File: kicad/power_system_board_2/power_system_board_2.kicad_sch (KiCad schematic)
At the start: 21 parts, among them J1 USB_C_Receptacle_USB2.0_16P, J2 Conn_01x04_Pin, Q1 NMOS - VN0109N3, Q3 PMOS - VP0106N3, U1 LM358

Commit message: Value updates
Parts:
- R3: value R -> 100K
- R4: value R -> 1.2M // 1.5M
- R5: value R -> 120
- R6: value R -> 90
- R7: value R -> 1M
- R8: value R -> 5M
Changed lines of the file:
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@@
 		(on_board yes)
 		(dnp no)
-		(fields_autoplaced yes)
 		(property "Reference" "R4"
-			(at 91.44 52.0699 0)
+			(at 78.994 51.308 0)
 			(effects
 				(font
@@
 			)
 		)
-		(property "Value" "R"
-			(at 91.44 54.6099 0)
+		(property "Value" "1.2M // 1.5M"
+			(at 73.152 53.34 0)
 			(effects
 				(font
@@
 			)
 		)
-		(property "Value" "R"
+		(property "Value" "120"
 			(at 102.87 68.5799 0)
 			(effects
@@
 		(on_board yes)
 		(dnp no)
-		(fields_autoplaced yes)
 		(property "Reference" "R3"
-			(at 91.44 35.5599 0)
+			(at 83.312 35.052 0)
 			(effects
 				(font
@@
 			)
 		)
-		(property "Value" "R"
-			(at 91.44 38.0999 0)
+		(property "Value" "100K"
+			(at 82.042 36.83 0)
 			(effects
 				(font
@@
 			)
 		)
-		(property "Value" "R"
+		(property "Value" "5M"
 			(at 132.08 54.6099 0)
 			(effects
@@
 			)
 		)
-		(property "Value" "R"
+		(property "Value" "1M"
 			(at 132.08 40.6399 0)
 			(effects
@@
 			)
 		)
-		(property "Value" "R"
+		(property "Value" "90"
 			(at 102.87 34.2899 0)
 			(effects

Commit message: schematic changes
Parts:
- removed R5: 120, symbol Device:R
- removed R7: 1M, symbol Device:R
- removed R8: 5M, symbol Device:R
- R3: value 100K -> 1M + 330k
- R4: value 1.2M // 1.5M -> 2M7 + 220k
- R6: value 90 -> 330
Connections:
- net GND: now also D1.2 (A)
- net at U1.5: now also Q3.2 (G)

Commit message: small changes
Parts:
- added Q2: PMOS - VP0106N3, symbol Simulation_SPICE:PMOS
- added R5: 330, symbol Device:R
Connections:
- net +BATT_UVLO: now also Q2.3 (S); no longer C1.1, C2.1, U3. (OUT)
- net VBUS: now also C1.1, C2.1, U3. (OUT), Q2.1 (D), R5.1
- new net: Q2.2 (G), R5.2
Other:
- note added: "Gate > Source, mosfet is open"

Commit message: Mouse
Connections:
- net -BATT: now also Q1.1 (D); no longer Q1.3 (S)
- net GND: now also Q1.3 (S); no longer Q1.1 (D)
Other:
- moved on the sheet: Q1
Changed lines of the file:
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@@
 	(symbol
 		(lib_id "Simulation_SPICE:NMOS")
-		(at 45.72 36.83 270)
+		(at 45.72 36.83 90)
+		(mirror x)
 		(unit 1)
 		(exclude_from_sim no)
@@
 		)
 		(property "Footprint" ""
-			(at 48.26 41.91 0)
+			(at 43.18 41.91 0)
 			(effects
 				(font
@@
 		)
 		(property "Datasheet" "https://ngspice.sourceforge.io/docs/ngspice-html-manual/manual.xhtml#cha_MOSFETs"
-			(at 33.02 36.83 0)
+			(at 58.42 36.83 0)
 			(effects
 				(font
@@
 		)
 		(property "Sim.Device" "NMOS"
-			(at 28.575 36.83 0)
+			(at 62.865 36.83 0)
 			(effects
 				(font
@@
 		)
 		(property "Sim.Type" "VDMOS"
-			(at 26.67 36.83 0)
+			(at 64.77 36.83 0)
 			(effects
 				(font
@@
 		)
 		(property "Sim.Pins" "1=D 2=G 3=S"
-			(at 30.48 36.83 0)
+			(at 60.96 36.83 0)
 			(effects
 				(font

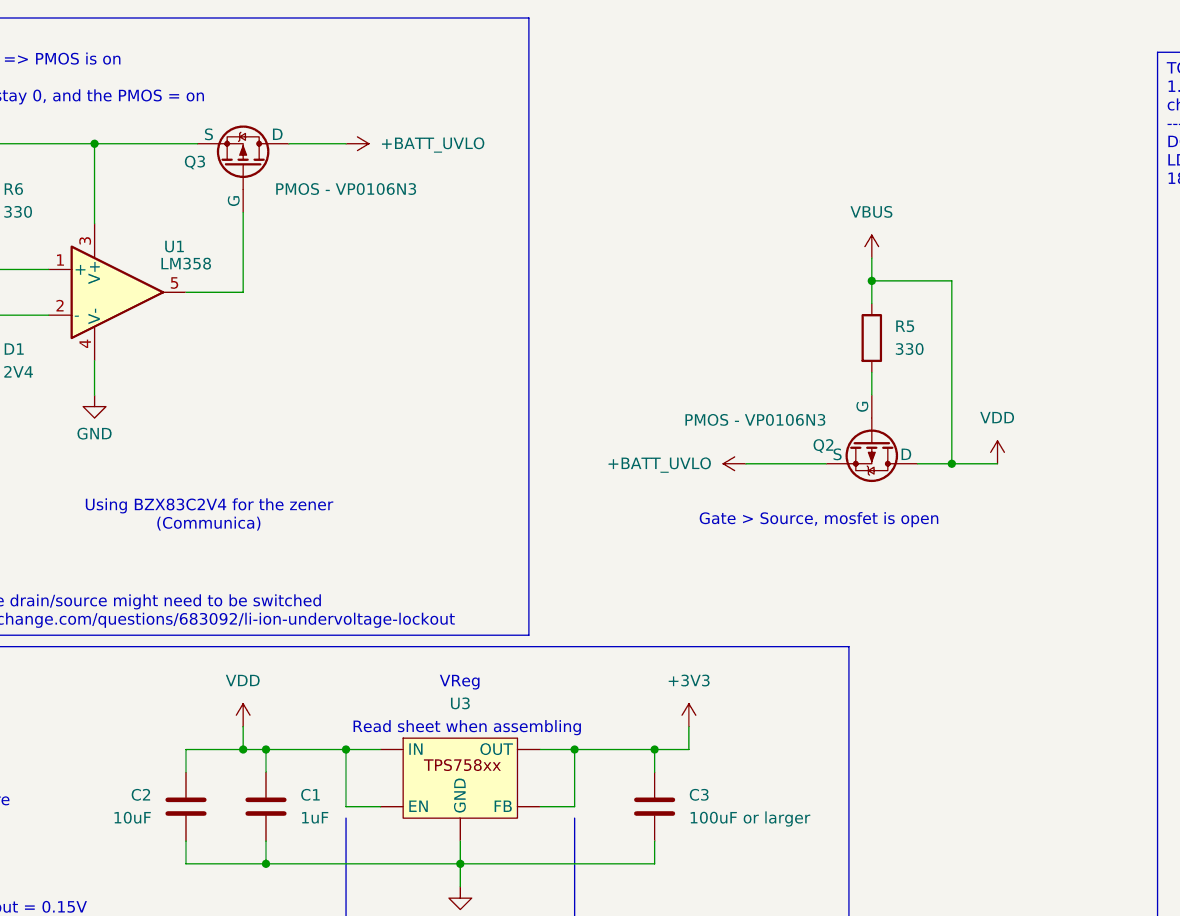
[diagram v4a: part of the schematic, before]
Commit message: Changes to circuit layout
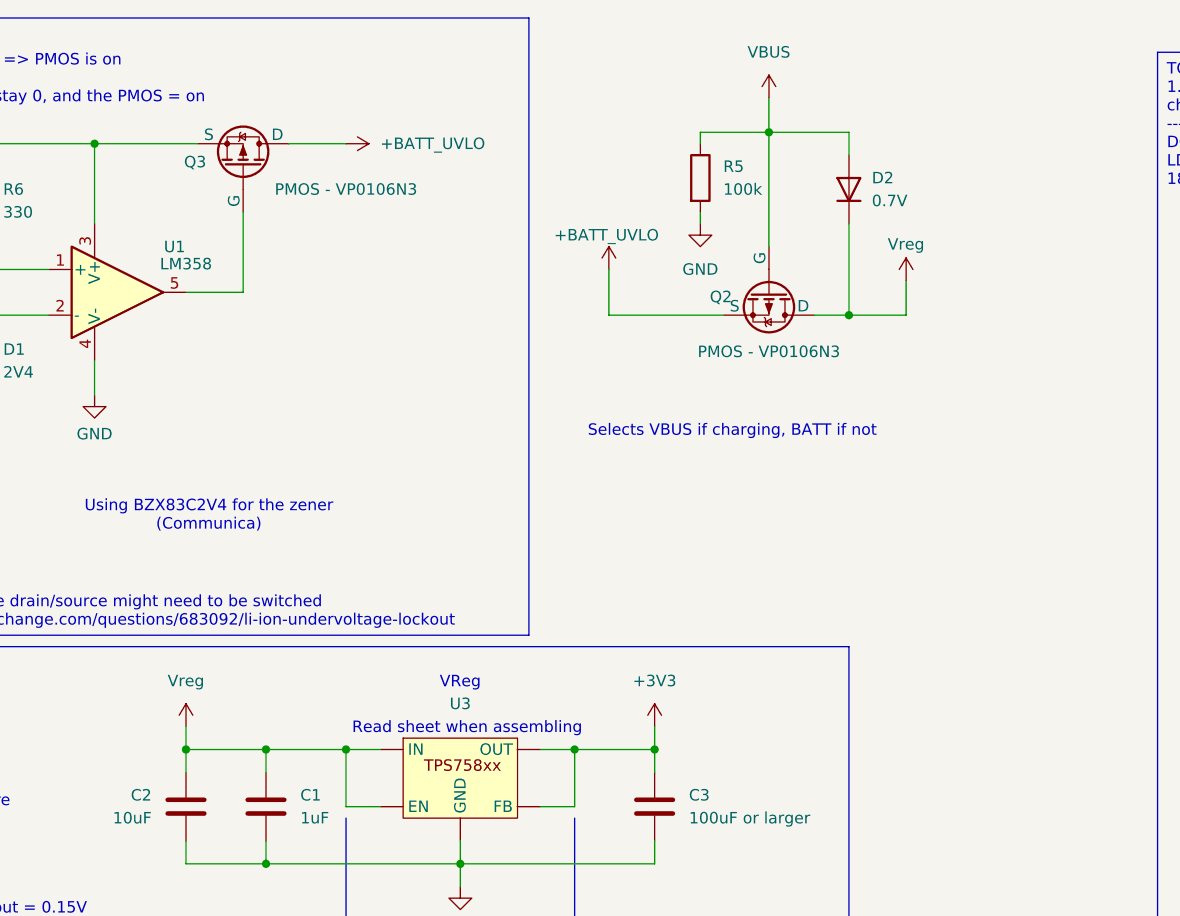
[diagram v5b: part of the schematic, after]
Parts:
- added D2: 0.7V, symbol Device:D
- R5: value 330 -> 100k
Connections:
- net GND: now also R5.2
- net VBUS: now also Q2.2 (G), D2.2 (A); no longer C1.1, C2.1, Q2.1 (D), U3. (OUT)
- new net Vreg: C1.1, C2.1, D2.1 (K), Q2.1 (D), U3. (OUT)
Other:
- note added: "Selects VBUS if charging, BATT if not"
- note removed: "Gate > Source, mosfet is open"
- moved on the sheet: Q2
